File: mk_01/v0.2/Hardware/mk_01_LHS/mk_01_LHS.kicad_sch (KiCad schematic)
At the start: 79 parts, among them SW1 SW_Push_Dual, U1 nice_nano

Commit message: Updated schematic
Updated schematic that was meant to be included in the last commit.
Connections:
- net at BATT1.1 (Pin_1): now also U1.23 (GND); no longer U1.24 (BATIN/P0.04)
- net at BATT1.2 (Pin_2): now also U1.24 (BATIN/P0.04); no longer U1.23 (GND)
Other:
- moved on the sheet: BATT1
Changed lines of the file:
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@@
     (pin "2")
   )
-  (symbol (lib_id "Connector_Generic:Conn_02x01") (at 303.53 90.17 270) (unit 1)
+  (symbol (lib_id "Connector_Generic:Conn_02x01") (at 303.53 92.71 90) (unit 1)
     (in_bom yes) (on_board yes) (fields_autoplaced)
     (property "Reference" "BATT1" (id 0) (at 305.562 90.5315 90)
-      (effects (font (size 1.27 1.27)) (justify left))
+      (effects (font (size 1.27 1.27)) (justify right))
     )
     (property "Value" "Conn_02x01" (id 1) (at 305.562 93.3066 90)
-      (effects (font (size 1.27 1.27)) (justify left))
+      (effects (font (size 1.27 1.27)) (justify right))
     )
-    (property "Footprint" "Capacitor_THT:C_Rect_L41.5mm_W20.0mm_P37.50mm_MKS4" (id 2) (at 303.53 90.17 0)
+    (property "Footprint" "Capacitor_THT:C_Rect_L41.5mm_W20.0mm_P37.50mm_MKS4" (id 2) (at 303.53 92.71 0)
       (effects (font (size 1.27 1.27)) hide)
     )
-    (property "Datasheet" "~" (id 3) (at 303.53 90.17 0)
+    (property "Datasheet" "~" (id 3) (at 303.53 92.71 0)
       (effects (font (size 1.27 1.27)) hide)
     )

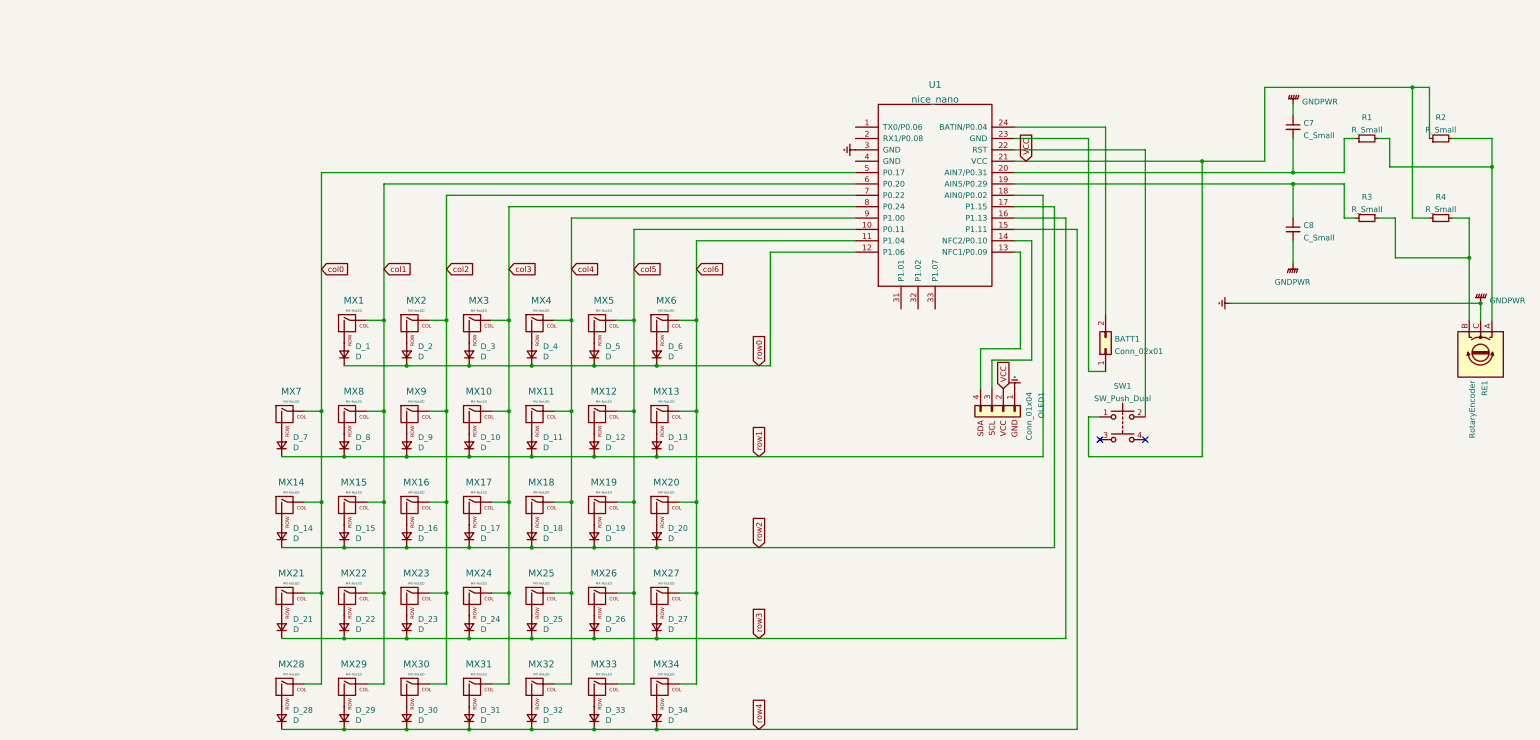
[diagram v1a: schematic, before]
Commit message: Finalising layout and troubleshooting round-tracks
The layout is pretty much complete, with all necessary components wired correctly. round-tracks keeps refusing to round one of the traces. A label free version has been added, however I'll probably remove this since it means two designs to constantly keep up to date.
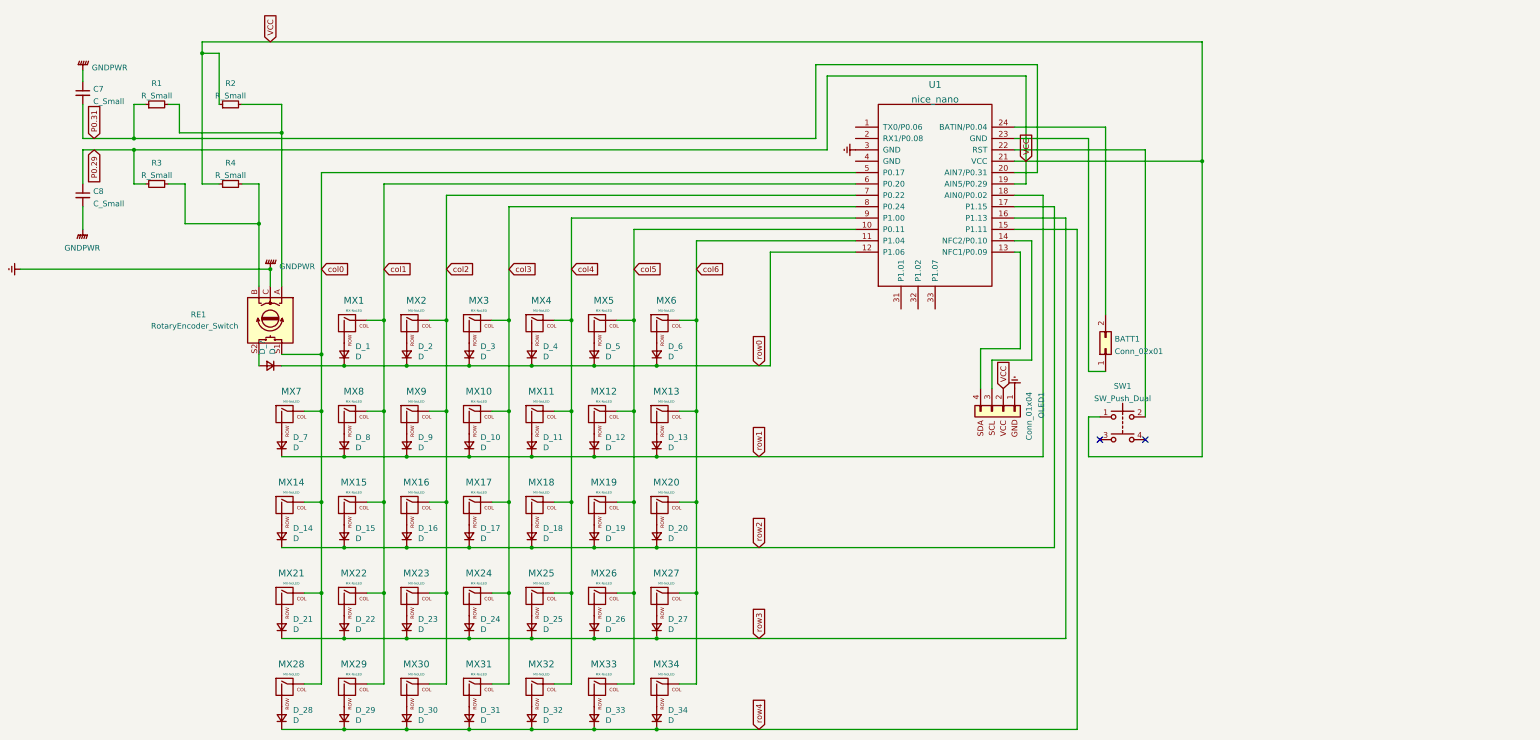
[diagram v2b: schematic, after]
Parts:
- removed RE1: RotaryEncoder, Rotary_Encoder:RotaryEncoder_Alps_EC12E_Vertical_H20mm, symbol Device:RotaryEncoder
- added D_?: D, Diode_SMD:D_SOD-123, symbol Device:D_Small
- added RE1: RotaryEncoder_Switch, Rotary_Encoder:RotaryEncoder_Alps_EC11E-Switch_Vertical_H20mm, symbol Device:RotaryEncoder_Switch
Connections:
- net VCC is gone; now on net P0.29: OLED1.2 (Pin_2), R2.1, R4.1, SW1.1, U1.21 (VCC)
- net Earth: now also RE1.C
- net col0: now also RE1.S1
- net row0: now also D_?.1 (K)
- net at R3.1, R4.2: now also RE1.B
- net P0.29: now reaches C8.1, R3.2, U1.19 (AIN5/P0.29)
- net P0.31: now reaches C7.2, R1.1, U1.20 (AIN7/P0.31)
- net at R1.2, R2.2: now also RE1.A
- new net: D_?.2 (A), RE1.S2
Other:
- moved on the sheet: C7, C8, R1, R2, R3, R4
